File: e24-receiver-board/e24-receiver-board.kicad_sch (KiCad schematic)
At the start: 21 parts, among them J1 505070-2422, J10 SPEAKER-, J11 GND1, J12 TRACK_RIGHT, J13 MOTOR+, J14 U+, J15 VCC, J16 LAMP_REAR, J17 AUX2, J18 AUX4, J19 AUX11, J2 TRACK_LEFT, J20 SPEAKER+, J21 GND2, J3 MOTOR-, J4 LAMP_FRONT, J5 CAP+, J6 AUX1, J7 AUX3, J8 AUX10, J9 AUX12

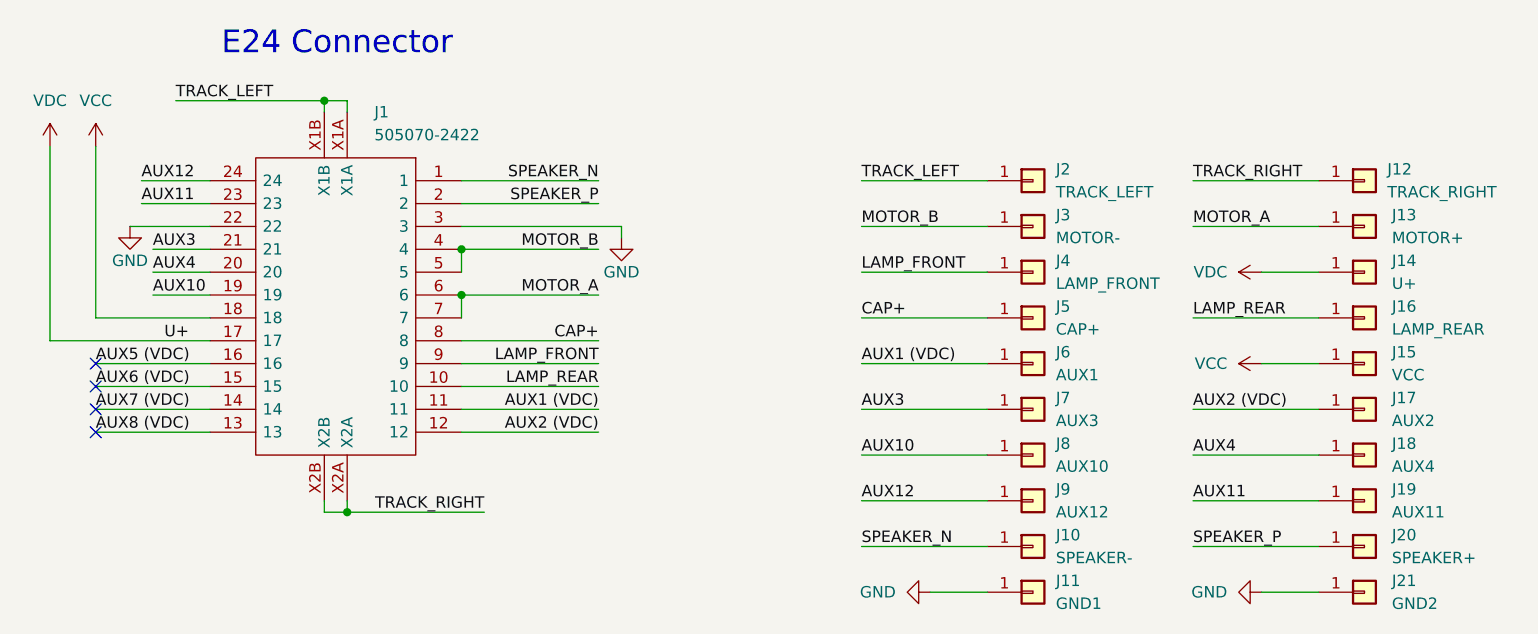
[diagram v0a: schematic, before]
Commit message: fix: space out higher power terminals
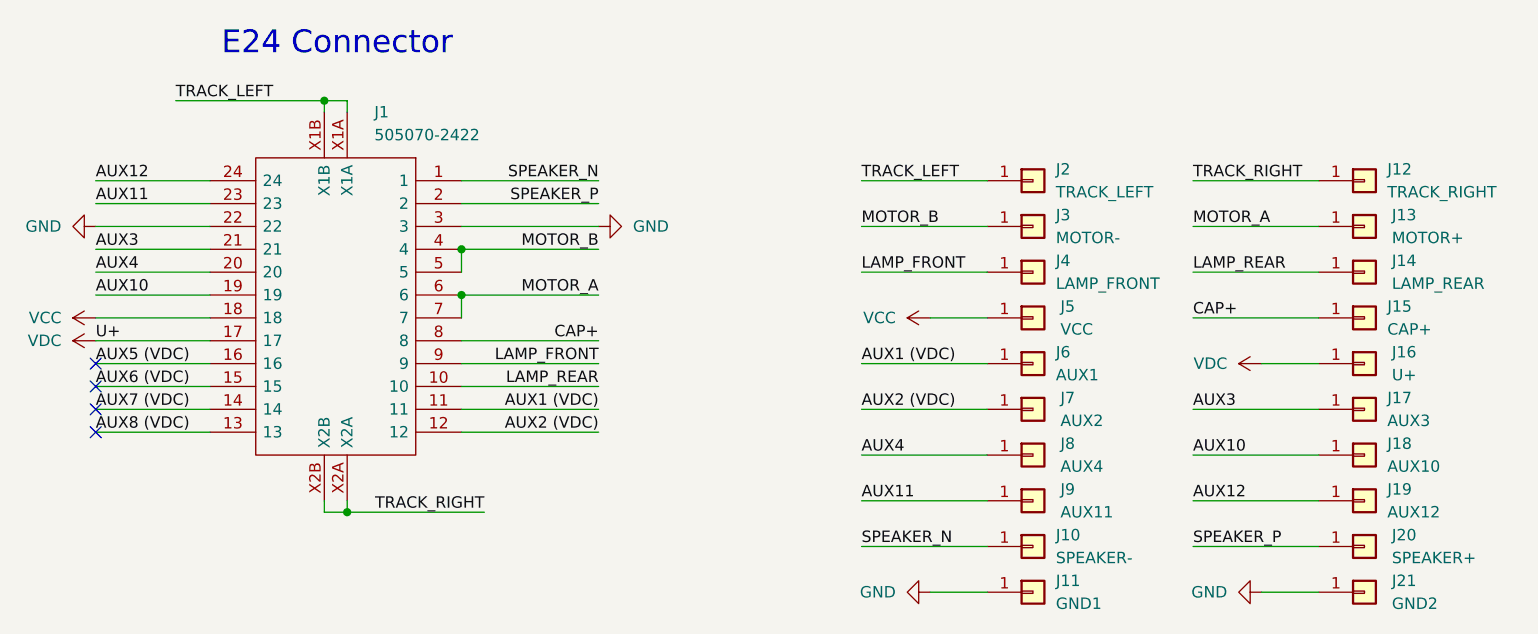
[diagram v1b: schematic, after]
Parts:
- J11, J12, J13, J2, J21, J3: footprint Connector_Wire:SolderWirePad_1x01_SMD_1x2mm -> Local Library:SolderWirePad_1x01_SMD_1.5x3mm
- renumbered J16 to J14, J5 to J15, J14 to J16, J7 to J17, J8 to J18, J9 to J19, J15 to J5, J17 to J7, J18 to J8, J19 to J9
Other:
- moved on the sheet: J14, J15, J16, J17, J18, J19, J5, J7, J8, J9
